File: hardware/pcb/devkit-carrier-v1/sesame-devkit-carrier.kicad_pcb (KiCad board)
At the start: 2 copper layers, 80 x 42 mm, 24 parts, among them J1 DevKit L, J2 DevKit R, J3 OLED, J4 IO, J5 IO2, J6 Battery pigtail, SW1 Switch, U1 Pololu D24V50F5

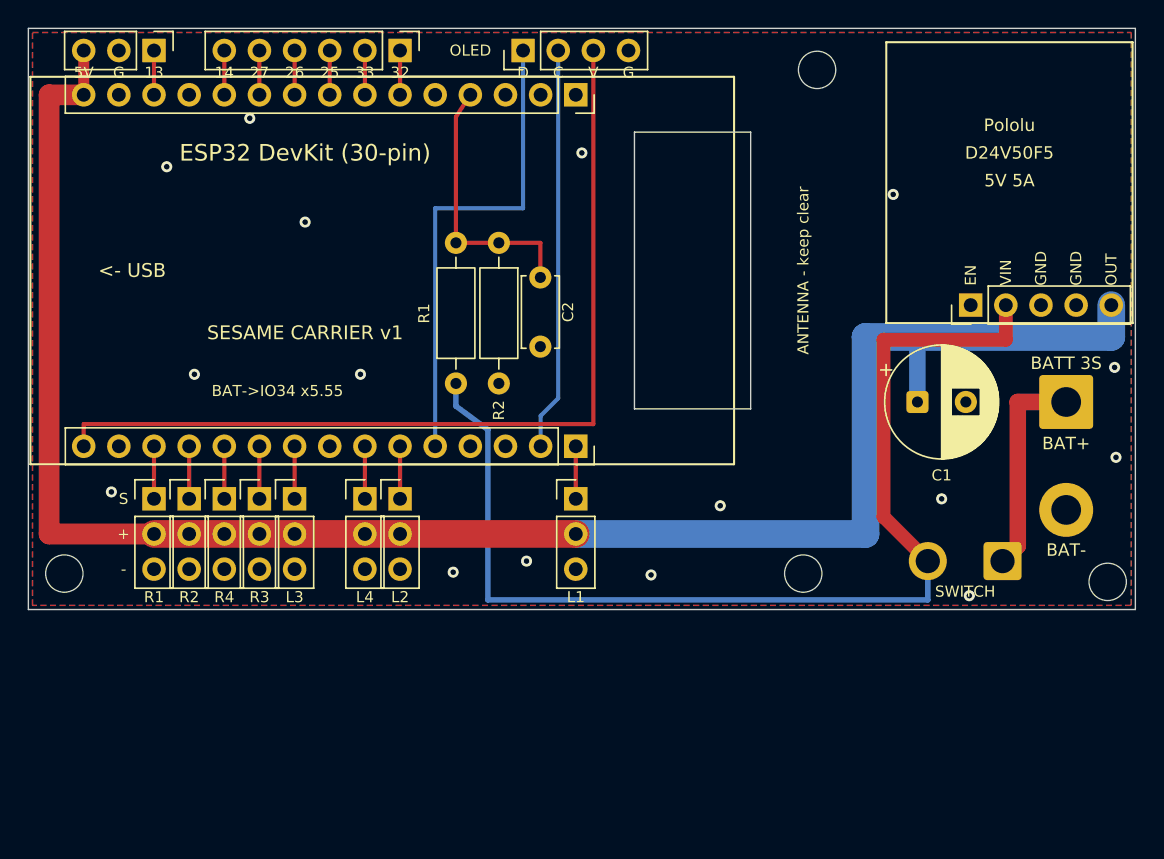
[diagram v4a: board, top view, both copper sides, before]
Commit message: Carrier PCB: DevKit antenna overhangs the board edge
Turn the DevKit around so its antenna end hangs past the left edge with
nothing under it; drop the antenna slot. USB now points inward (flash the
DevKit before plugging it in). Servo headers move to the top strip and the
I/O + OLED headers to the bottom, still each in line with its pin. Board
shrinks to 69 x 42 mm.

Co-Authored-By: Claude Opus 5.5 <noreply@anthropic.com>
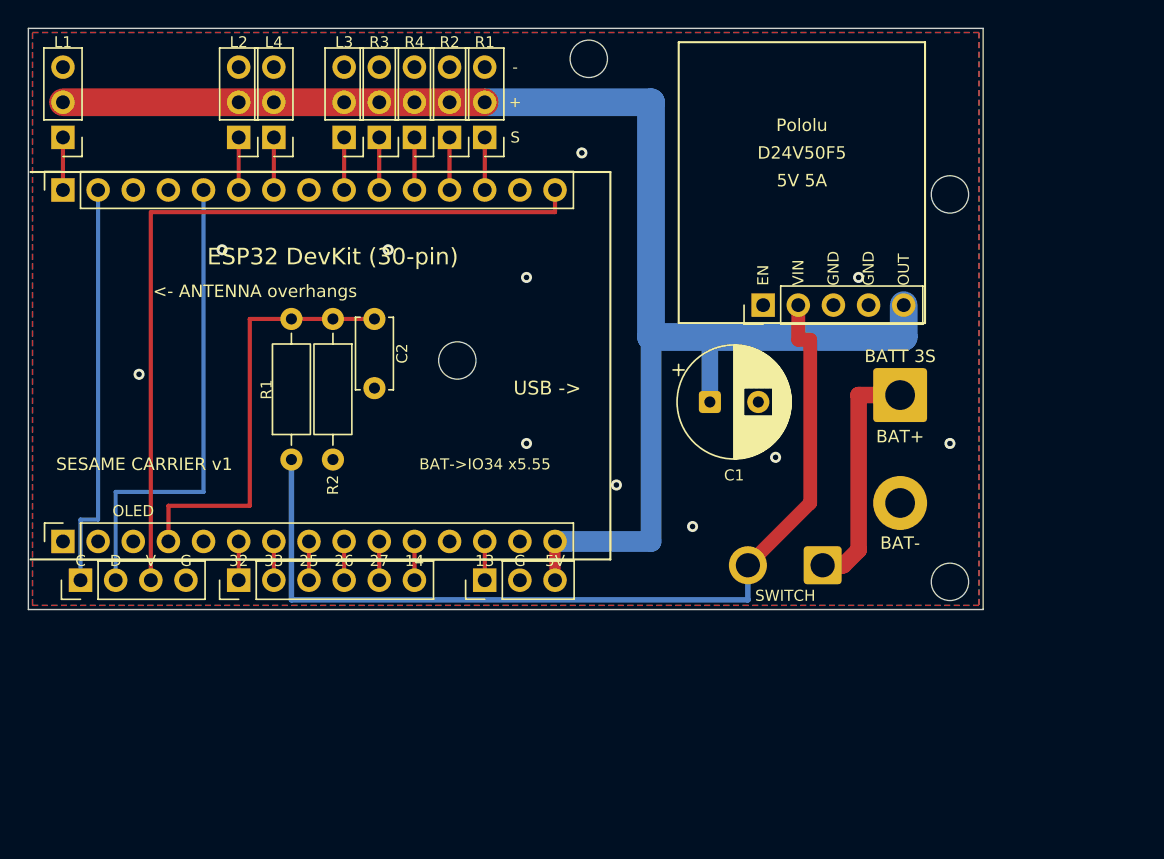
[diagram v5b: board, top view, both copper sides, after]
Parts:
- moved H1 53.1 mm to (40.5, 2.20)
- moved J3 49.9 mm to (3.77, 39.9)
- moved H4 49.6 mm to (31.0, 24.0)
- moved J1 49.1 mm to (2.50, 37.1), turned to 90 degrees
- moved S1 45.3 mm to (2.50, 7.88), turned to 180 degrees
- moved J5 45.1 mm to (33.0, 39.9), turned to 90 degrees
- moved J2 41.4 mm to (2.50, 11.7), turned to 90 degrees
- moved J4 40.0 mm to (15.2, 39.9), turned to 90 degrees
- moved S8 35.4 mm to (33.0, 7.88), turned to 180 degrees
- moved S7 32.2 mm to (30.4, 7.88), turned to 180 degrees
- moved S6 29.5 mm to (27.9, 7.88), turned to 180 degrees
- moved S2 28.6 mm to (15.2, 7.88), turned to 180 degrees
- moved S5 27.5 mm to (25.4, 7.88), turned to 180 degrees
- moved S3 26.9 mm to (17.7, 7.88), turned to 180 degrees
- moved S4 26.4 mm to (22.8, 7.88), turned to 180 degrees
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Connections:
- J3 pad 1: SDA -> SCL
- J3 pad 2: SCL -> SDA
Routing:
- net +5V: track 135.4 -> 109.2 mm
- net VBAT_SW: track 80.1 -> 67.2 mm
- net BAT_SENSE: track 19.6 -> 31.0 mm
- net +3V3: track 65.4 -> 57.4 mm
- net VBAT: track 15.5 -> 17.3 mm
- net GND: vias 16 -> 11
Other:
- board size 80 x 42 mm -> 69 x 42 mm
- board text added: "<- ANTENNA overhangs"
- board text added: "USB ->"
- board text removed: "<- USB"
- board text removed: "ANTENNA - keep clear"

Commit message: Carrier PCB: Sesame 'cute' face art on both sides
Face is read pixel-for-pixel from firmware/face-bitmaps.h at build time.
Battery-sense divider moved toward the DevKit's USB end to clear room for
the big back-side face.

Co-Authored-By: Claude Opus 5.5 <noreply@anthropic.com>
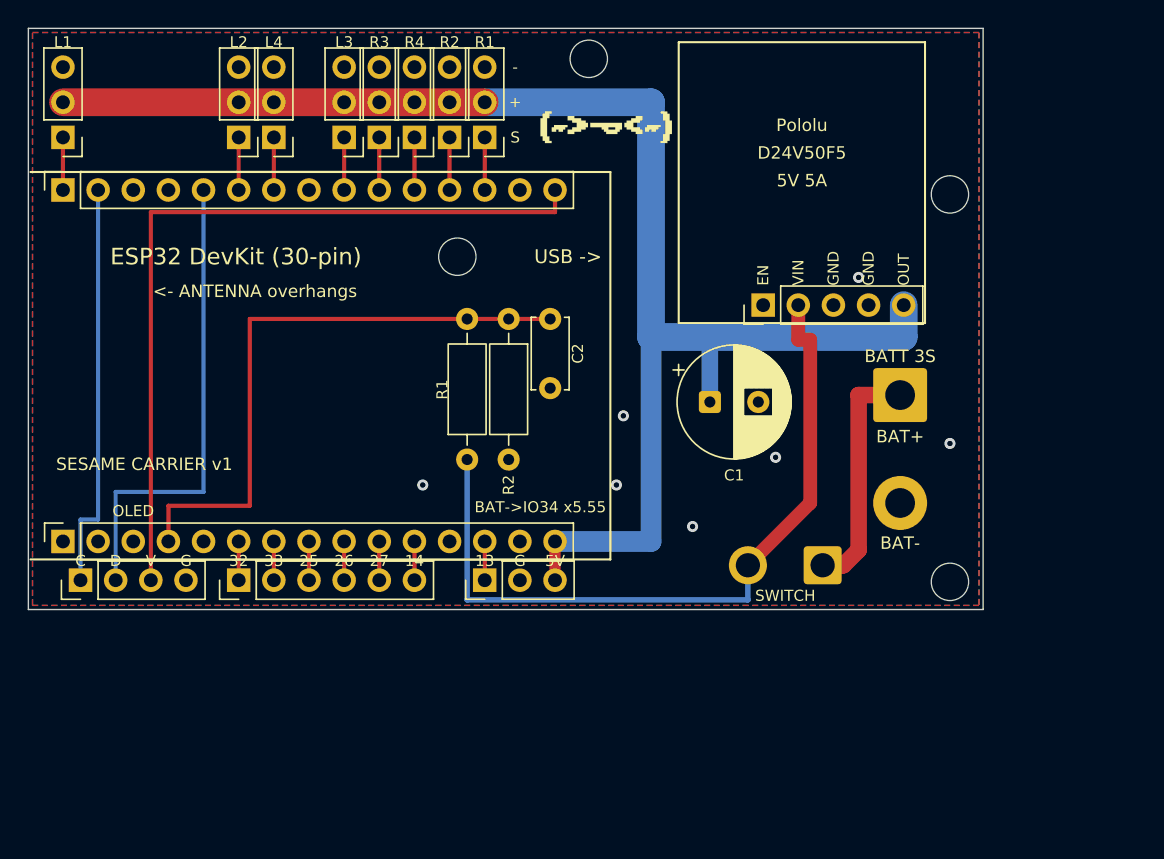
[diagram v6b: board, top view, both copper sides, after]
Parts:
- moved C2 12.7 mm to (37.7, 21.0)
- moved R1 12.7 mm to (31.7, 31.2)
- moved R2 12.7 mm to (34.7, 21.0)
- moved H4 7.50 mm to (31.0, 16.5)
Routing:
- net BAT_SENSE: track 31.0 -> 43.7 mm
- net VBAT_SW: track 67.2 -> 54.5 mm
- net GND: vias 11 -> 7
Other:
- board text added: "DevKit carrier v1"
- board text added: "SESAME"

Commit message: Carrier PCB: electrical audit, widen battery path, double servo 5V rail
Add audit.py, an independent check of netlist vs spec, firmware pin
mapping, current capacity, ground fill, polarity and labels. Battery-side
traces widened to 1.5 mm (3.2 A) for the ~2.8 A peak regulator input; servo
5V rail doubled on the back layer (2 x 2.0 mm).

Co-Authored-By: Claude Opus 5.5 <noreply@anthropic.com>
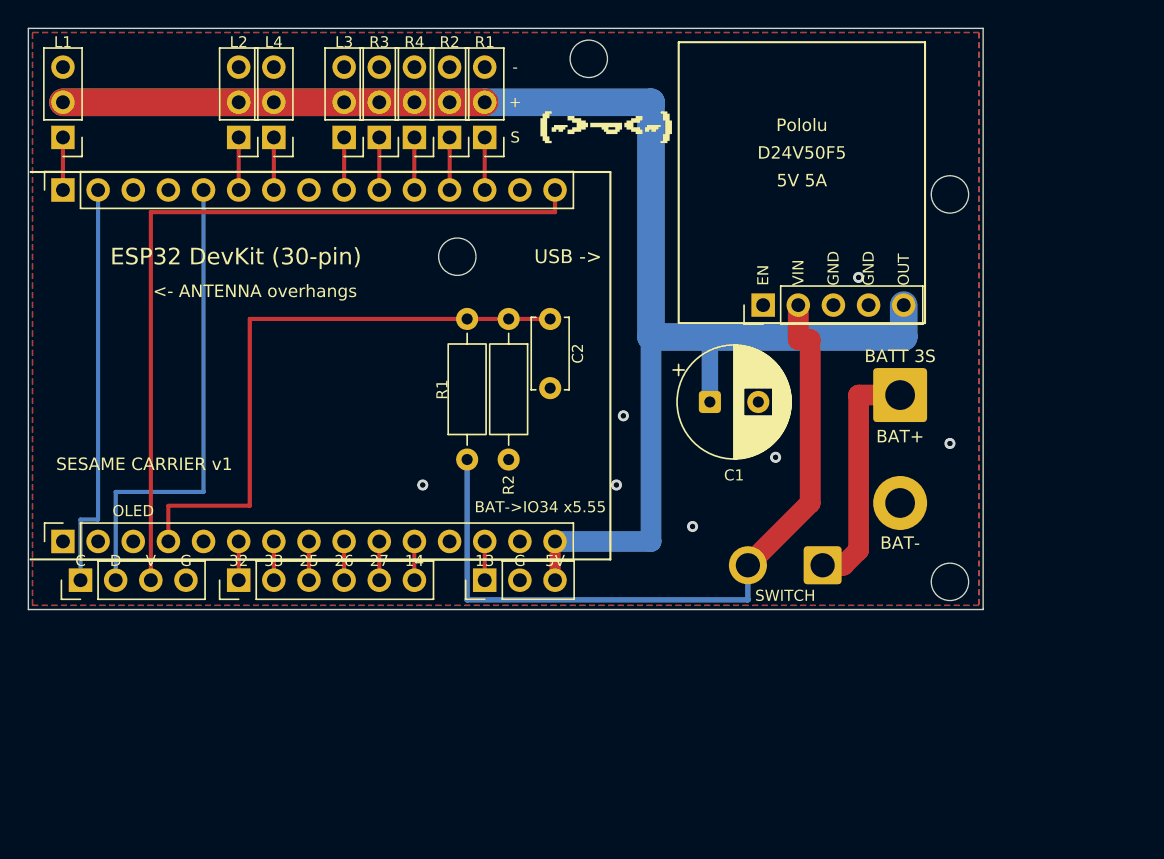
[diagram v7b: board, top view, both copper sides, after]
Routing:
- net +5V: track 109.2 -> 139.7 mm

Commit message: Carrier PCB: Pololu footprint from official dimension drawing
Pin row and outline now follow Pololu's D24V50F5 drawing (0J1436): EN 5.73 mm
from the left edge (was estimated 6.1 mm from a photo), row 1.27 mm up.

Co-Authored-By: Claude Opus 5.5 <noreply@anthropic.com>
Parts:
- moved U1 0.37 mm to (52.7, 20.0)
